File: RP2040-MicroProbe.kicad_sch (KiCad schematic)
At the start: 66 parts, among them J1 CONN_MCU_JTAG, J10 CONN_USB, J2 CONN_MCU_UART, J3 CONN_DBG_COMB, J4 CONN_3V3_JUMPER, J7 CONN_DBG_JTAG, SW1 BOOTSEL, U1 W25Q128JVS, U2 RP2040, U3 74AUP1T17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

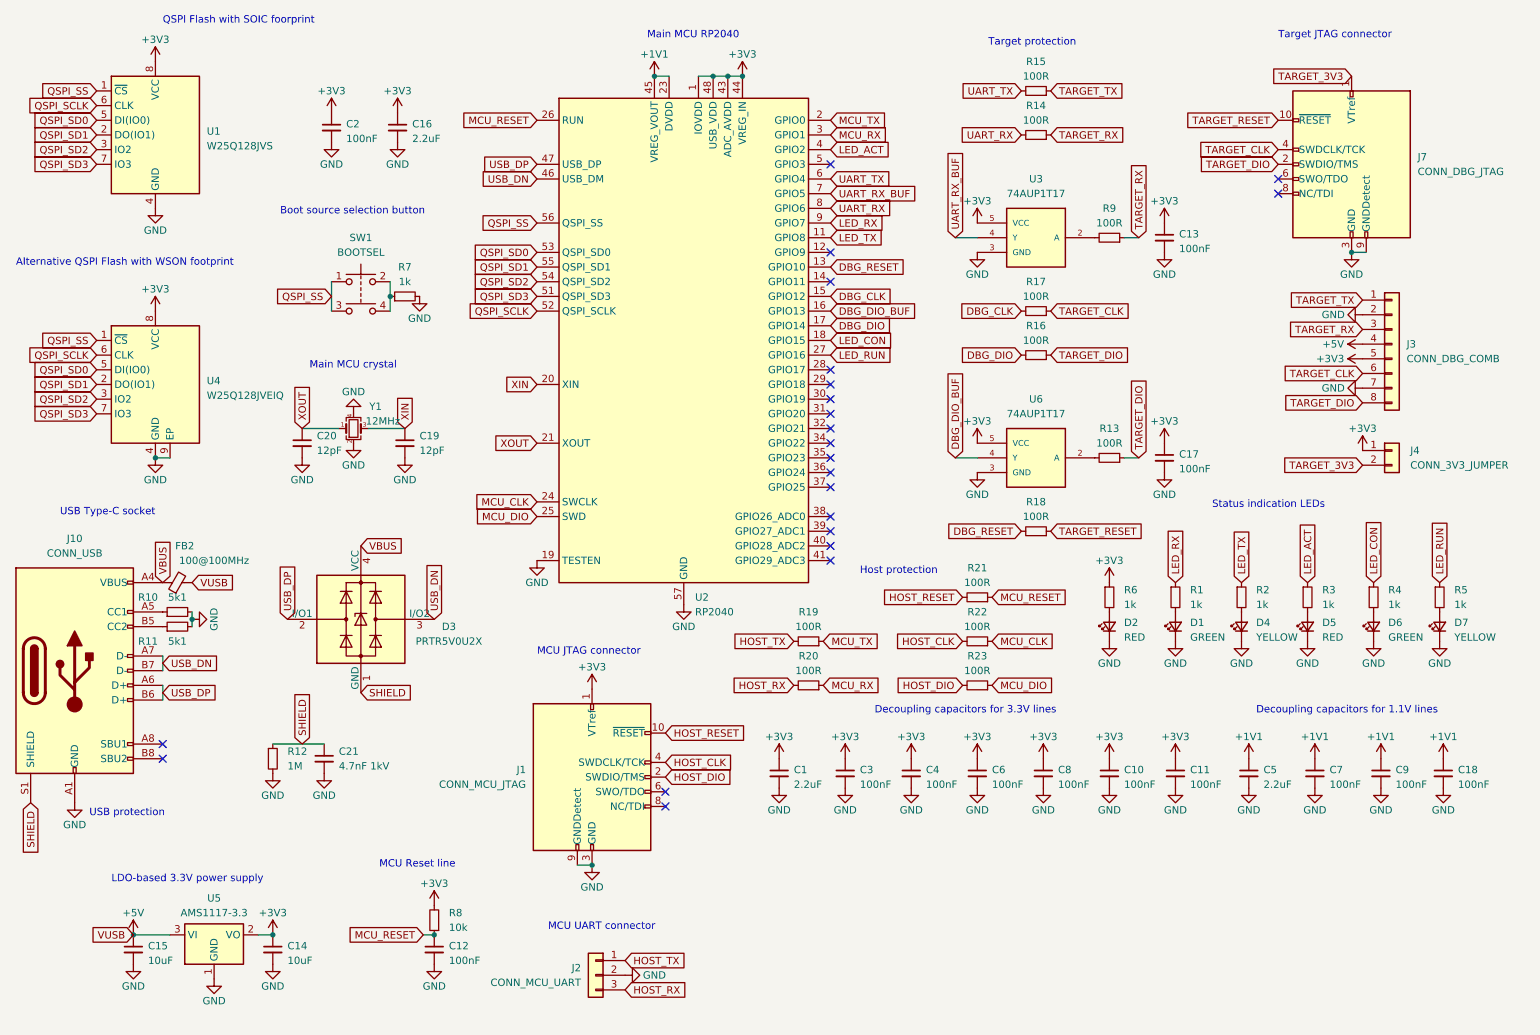
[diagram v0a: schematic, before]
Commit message: Cleanup components a bit. Changed few components and footprints.
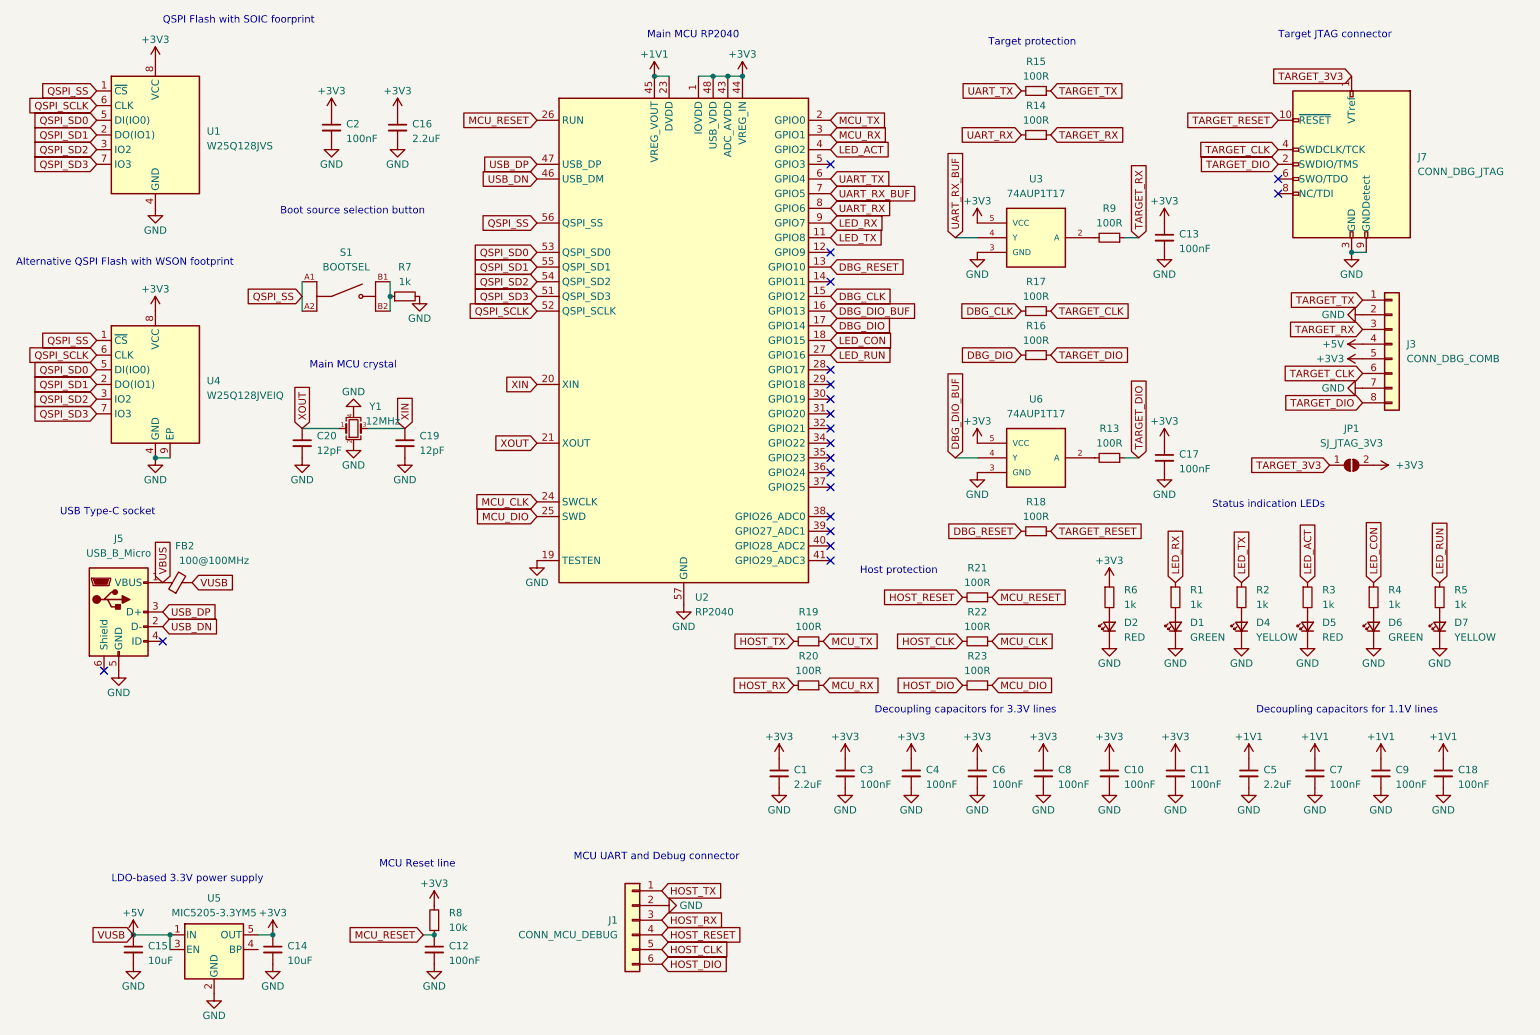
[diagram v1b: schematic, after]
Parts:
- removed C21: 4.7nF 1kV, Capacitor_SMD:C_1206_3216Metric, symbol Device:C_Small
- removed D3: PRTR5V0U2X, Package_TO_SOT_SMD:SOT-143, symbol Power_Protection:PRTR5V0U2X
- removed J1: CONN_MCU_JTAG, Connector_PinHeader_1.27mm:PinHeader_2x05_P1.27mm_Vertical, symbol Connector:Conn_ARM_JTAG_SWD_10
- removed J10: CONN_USB, Connector_USB:USB_C_Receptacle_HRO_TYPE-C-31-M-12, symbol Connector:USB_C_Receptacle_USB2.0
- removed J2: CONN_MCU_UART, Connector_PinHeader_2.54mm:PinHeader_1x03_P2.54mm_Vertical, symbol Connector_Generic:Conn_01x03
- removed J4: CONN_3V3_JUMPER, Connector_PinHeader_2.54mm:PinHeader_1x02_P2.54mm_Vertical, symbol Connector_Generic:Conn_01x02
- removed R10, R11: 5k1, Resistor_SMD:R_0402_1005Metric, symbol Device:R_Small
- removed R12: 1M, Resistor_SMD:R_0603_1608Metric, symbol Device:R_Small
- removed SW1: BOOTSEL, PCM_4ms_Switch:Button_Tact_Sqkg, symbol Switch:SW_Push_Dual
- removed U5: AMS1117-3.3, Package_TO_SOT_SMD:SOT-223-3_TabPin2, symbol Regulator_Linear:AMS1117-3.3
- added J1: CONN_MCU_DEBUG, Connector_PinHeader_2.54mm:PinHeader_1x06_P2.54mm_Vertical, symbol Connector_Generic:Conn_01x06
- added J5: USB_B_Micro, Connector_USB:USB_Micro-B_Molex_47346-0001, symbol Connector:USB_B_Micro
- added JP1: SJ_JTAG_3V3, Jumper:SolderJumper-2_P1.3mm_Open_TrianglePad1.0x1.5mm, symbol Jumper:SolderJumper_2_Open
- added S1: BOOTSEL, lib:SW_EVPBB0AAB000, symbol EVPBB0AAB000:EVPBB0AAB000
- added U5: MIC5205-3.3YM5, Package_TO_SOT_SMD:SOT-23-5, symbol Regulator_Linear:MIC5205-3.3YM5
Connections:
- net +3V3: now also JP1.2 (B), U5.5 (OUT)
- net +5V: now also U5.1 (IN), U5.3 (EN)
- net GND: now also J1.2 (Pin_2), J5.5 (GND), U5.2 (GND)
- net HOST_CLK: now also J1.5 (Pin_5)
- net HOST_DIO: now also J1.6 (Pin_6)
- net HOST_RESET: now also J1.4 (Pin_4)
- net HOST_RX: now also J1.3 (Pin_3)
- net HOST_TX: now also J1.1 (Pin_1)
- net QSPI_SS: now also S1.A1, S1.A2
- net TARGET_3V3: now also JP1.1 (A)
- net USB_DN: now also J5.2 (D-)
- net USB_DP: now also J5.3 (D+)
- net VBUS: now also J5.1 (VBUS)
- net at R7.1: now also S1.B1, S1.B2
- no-connect marks 22 -> 20
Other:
- note added: "MCU UART and Debug connector"
- note removed: "MCU JTAG connector"
- note removed: "MCU UART connector"
- note removed: "USB protection"
- title: RP2040-DebugProbe-0010 -> RP2040-MicroProbe-0010

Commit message: Moved stuff around
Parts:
- removed R19, R20, R21, R22, R23: 100R, Resistor_SMD:R_0402_1005Metric, symbol Device:R_Small
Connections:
- net MCU_CLK is gone; now on net HOST_CLK: U2.24 (SWCLK)
- net MCU_DIO is gone; now on net HOST_DIO: U2.25 (SWD)
- net MCU_RESET is gone; now on net HOST_RESET: C12.1, R8.1, U2.26 (RUN)
- net MCU_RX is gone; now on net HOST_RX: U2.3 (GPIO1)
- net MCU_TX is gone; now on net HOST_TX: U2.2 (GPIO0)
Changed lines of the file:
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@@
   (no_connect (at 166.37 101.6))
   (no_connect (at 166.37 45.72))
+  (wire (pts (xy 160.02 128.27) (xy 165.1 128.27))
+    (stroke (width 0) (type default))
+  )
   (wire (pts (xy 86.36 91.44) (xy 92.71 91.44))
     (stroke (width 0) (type default))
   )
+  (wire (pts (xy 160.02 135.89) (xy 165.1 135.89))
+    (stroke (width 0) (type default))
+  )
   (wire (pts (xy 219.71 96.52) (xy 217.17 96.52))
     (stroke (width 0) (type default))
   )
+  (wire (pts (xy 189.23 120.65) (xy 194.31 120.65))
+    (stroke (width 0) (type default))
+  )
   (wire (pts (xy 74.93 66.04) (xy 74.93 71.12))
     (stroke (width 0) (type default))
@@
     (stroke (width 0) (type default))
   )
+  (wire (pts (xy 189.23 135.89) (xy 194.31 135.89))
+    (stroke (width 0) (type default))
+  )
   (wire (pts (xy 95.885 179.07) (xy 97.79 179.07))
     (stroke (width 0) (type default))
@@
   )
   (wire (pts (xy 187.96 58.42) (xy 191.77 58.42))
+    (stroke (width 0) (type default))
+  )
+  (wire (pts (xy 189.23 128.27) (xy 194.31 128.27))
     (stroke (width 0) (type default))
   )
@@
         (path "/9a38a81c-7302-494f-9784-2ab4342a0a1d"
           (reference "#PWR031") (unit 1)
-        )
-      )
-    )
-  )
-  (symbol (lib_id "Device:R_Small") (at 162.56 135.89 270) (mirror x) (unit 1)
-    (in_bom yes) (on_board yes) (dnp no) (fields_autoplaced)
-    (property "Reference" "R20" (at 162.56 130.81 90)
-      (effects (font (size 1.27 1.27)))
-    )
-    (property "Value" "100R" (at 162.56 133.35 90)
-      (effects (font (size 1.27 1.27)))
-    )
-    (property "Footprint" "Resistor_SMD:R_0402_1005Metric" (at 162.56 135.89 0)
-      (effects (font (size 1.27 1.27)) hide)
-    )
-    (property "Datasheet" "~" (at 162.56 135.89 0)
-      (effects (font (size 1.27 1.27)) hide)
-    )
-    (pin "1")
-    (pin "2")
-    (instances
-      (project "RP2040-MicroProbe"
-        (path "/9a38a81c-7302-494f-9784-2ab4342a0a1d"
-          (reference "R20") (unit 1)
         )
       )
@@
     )
   )
-  (symbol (lib_id "Device:R_Small") (at 191.77 120.65 270) (mirror x) (unit 1)
-    (in_bom yes) (on_board yes) (dnp no) (fields_autoplaced)
-    (property "Reference" "R21" (at 191.77 115.57 90)
-      (effects (font (size 1.27 1.27)))
-    )
-    (property "Value" "100R" (at 191.77 118.11 90)
-      (effects (font (size 1.27 1.27)))
-    )
-    (property "Footprint" "Resistor_SMD:R_0402_1005Metric" (at 191.77 120.65 0)
-      (effects (font (size 1.27 1.27)) hide)
-    )
-    (property "Datasheet" "~" (at 191.77 120.65 0)
-      (effects (font (size 1.27 1.27)) hide)
-    )
-    (pin "1")
-    (pin "2")
-    (instances
-      (project "RP2040-MicroProbe"
-        (path "/9a38a81c-7302-494f-9784-2ab4342a0a1d"
-          (reference "R21") (unit 1)
-        )
-      )
-    )
-  )
   (symbol (lib_id "power:GND") (at 157.48 153.67 0) (unit 1)
     (in_bom yes) (on_board yes) (dnp no)
@@
     )
   )
-  (symbol (lib_id "Device:R_Small") (at 162.56 128.27 270) (mirror x) (unit 1)
-    (in_bom yes) (on_board yes) (dnp no) (fields_autoplaced)
-    (property "Reference" "R19" (at 162.56 123.19 90)
-      (effects (font (size 1.27 1.27)))
-    )
-    (property "Value" "100R" (at 162.56 125.73 90)
-      (effects (font (size 1.27 1.27)))
-    )
-    (property "Footprint" "Resistor_SMD:R_0402_1005Metric" (at 162.56 128.27 0)
-      (effects (font (size 1.27 1.27)) hide)
-    )
-    (property "Datasheet" "~" (at 162.56 128.27 0)
-      (effects (font (size 1.27 1.27)) hide)
-    )
-    (pin "1")
-    (pin "2")
-    (instances
-      (project "RP2040-MicroProbe"
-        (path "/9a38a81c-7302-494f-9784-2ab4342a0a1d"
-          (reference "R19") (unit 1)
-        )
-      )
-    )
-  )
   (symbol (lib_id "power:GND") (at 43.18 133.35 0) (unit 1)
     (in_bom yes) (on_board yes) (dnp no)
@@
         (path "/9a38a81c-7302-494f-9784-2ab4342a0a1d"
           (reference "R2") (unit 1)
-        )
-      )
-    )
-  )
-  (symbol (lib_id "Device:R_Small") (at 191.77 128.27 270) (mirror x) (unit 1)
-    (in_bom yes) (on_board yes) (dnp no) (fields_autoplaced)
-    (property "Reference" "R22" (at 191.77 123.19 90)
-      (effects (font (size 1.27 1.27)))
-    )
-    (property "Value" "100R" (at 191.77 125.73 90)
-      (effects (font (size 1.27 1.27)))
-    )
-    (property "Footprint" "Resistor_SMD:R_0402_1005Metric" (at 191.77 128.27 0)
-      (effects (font (size 1.27 1.27)) hide)
-    )
-    (property "Datasheet" "~" (at 191.77 128.27 0)
-      (effects (font (size 1.27 1.27)) hide)
-    )
-    (pin "1")
-    (pin "2")
-    (instances
-      (project "RP2040-MicroProbe"
-        (path "/9a38a81c-7302-494f-9784-2ab4342a0a1d"
-          (reference "R22") (unit 1)
         )
       )
@@
         )
       )
-    )
-  )
-  (symbol (lib_id "Device:R_Small") (at 191.77 135.89 270) (mirror x) (unit 1)
-    (in_bom yes) (on_board yes) (dnp no) (fields_autoplaced)
-    (property "Reference" "R23" (at 191.77 130.81 90)
-      (effects (font (size 1.27 1.27)))
-    )
-    (property "Value" "100R" (at 191.77 133.35 90)
-      (effects (font (size 1.27 1.27)))
-    )
-    (property "Footprint" "Resistor_SMD:R_0402_1005Metric" (at 191.77 135.89 0)
-      (effects (font (size 1.27 1.27)) hide)
-    )
-    (property "Datasheet" "~" (at 191.77 135.89 0)
-      (effects (font (size 1.27 1.27)) hide)
-    )
-    (pin "1")
-    (pin "2")
-    (instances
-      (project "RP2040-MicroProbe"
-        (path "/9a38a81c-7302-494f-9784-2ab4342a0a1d"
-          (reference "R23") (unit 1)
-        )
-      )

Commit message: Moved stuff around
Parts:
- removed C3, C7: 100nF, Capacitor_SMD:C_0402_1005Metric, symbol Device:C_Small
- removed J3: CONN_DBG_COMB, Connector_PinHeader_2.54mm:PinHeader_1x08_P2.54mm_Vertical, symbol Connector_Generic:Conn_01x08
- removed R13, R14, R15, R16, R17, R18, R9: 100R, Resistor_SMD:R_0402_1005Metric, symbol Device:R_Small
- added J2: CONN_DBG_COMB, Connector_PinSocket_2.54mm:PinSocket_1x07_P2.54mm_Vertical, symbol Connector_Generic:Conn_01x07
- added JP2: SJ_RESET, Jumper:SolderJumper-2_P1.3mm_Open_TrianglePad1.0x1.5mm, symbol Jumper:SolderJumper_2_Open
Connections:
- net TARGET_CLK is gone; now on net DBG_CLK: J7.4 (SWDCLK/TCK)
- net TARGET_DIO is gone; now on net DBG_DIO: J7.2 (SWDIO/TMS)
- net UART_RX is gone; now on net TARGET_RX: U2.8 (GPIO6)
- net UART_TX is gone; now on net TARGET_TX: U2.6 (GPIO4)
- net +3V3: now also J2.4 (Pin_4)
- net DBG_CLK: now also J2.5 (Pin_5)
- net DBG_DIO: now also U6.2 (A), J2.7 (Pin_7)
- net DBG_RESET: now also JP2.1 (A)
- net GND: now also J2.2 (Pin_2), J2.6 (Pin_6)
- net TARGET_RESET: now also JP2.2 (B)
- net TARGET_RX: now also U3.2 (A), J2.3 (Pin_3)
- net TARGET_TX: now also J2.1 (Pin_1)
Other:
- note added: "Host connections"
- note added: "Target connections"
- note removed: "Host protection"
- note removed: "Target protection"
- moved on the sheet: C1, C13, C17, C18, C9

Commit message: Moved stuff around
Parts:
- J7: footprint Connector_PinHeader_1.27mm:PinHeader_2x05_P1.27mm_Vertical -> Connector_PinHeader_1.27mm:PinHeader_2x05_P1.27mm_Vertical_SMD
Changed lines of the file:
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@@
       (effects (font (size 1.27 1.27)) (justify right))
     )
-    (property "Footprint" "Connector_PinHeader_1.27mm:PinHeader_2x05_P1.27mm_Vertical" (at 256.54 45.72 0)
+    (property "Footprint" "Connector_PinHeader_1.27mm:PinHeader_2x05_P1.27mm_Vertical_SMD" (at 256.54 45.72 0)
       (effects (font (size 1.27 1.27)) hide)
     )

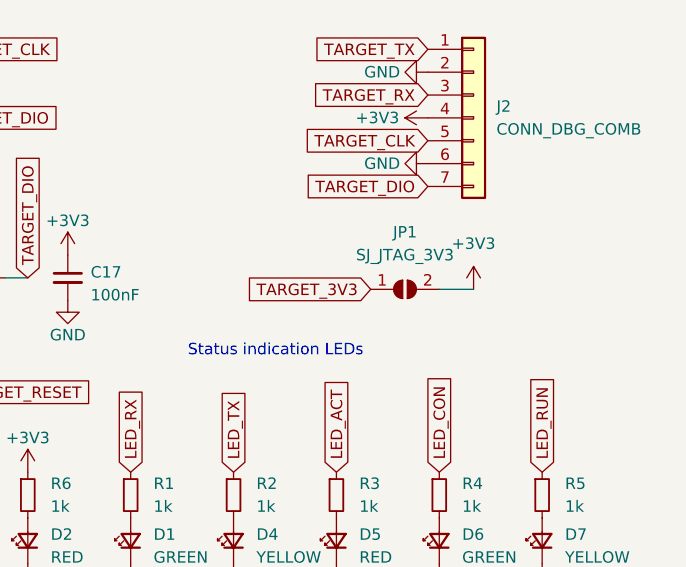
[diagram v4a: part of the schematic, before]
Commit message: Added traces and vias
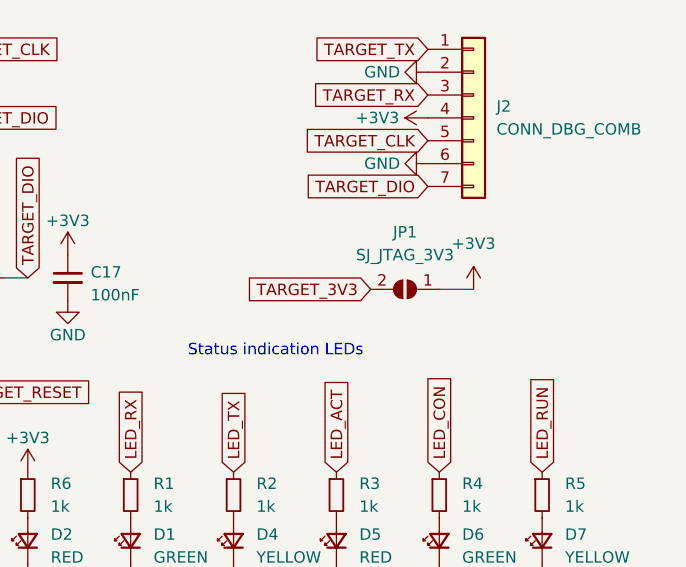
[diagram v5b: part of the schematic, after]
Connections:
- net +3V3: now also JP1.1 (A); no longer JP1.2 (B)
- net TARGET_3V3: now also JP1.2 (B); no longer JP1.1 (A)
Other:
- moved on the sheet: JP1
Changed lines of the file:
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@@
   (title_block
     (title "RP2040-MicroProbe-0010")
-    (date "2023-12-18")
+    (date "2023-12-19")
     (rev "1.0")
     (company "(c) 2023 Andriy Golovnya")
@@
     )
   )
-  (symbol (lib_id "Jumper:SolderJumper_2_Open") (at 256.54 97.79 0) (unit 1)
+  (symbol (lib_id "Jumper:SolderJumper_2_Open") (at 256.54 97.79 180) (unit 1)
     (in_bom yes) (on_board yes) (dnp no) (fields_autoplaced)
     (property "Reference" "JP1" (at 256.54 91.44 0)

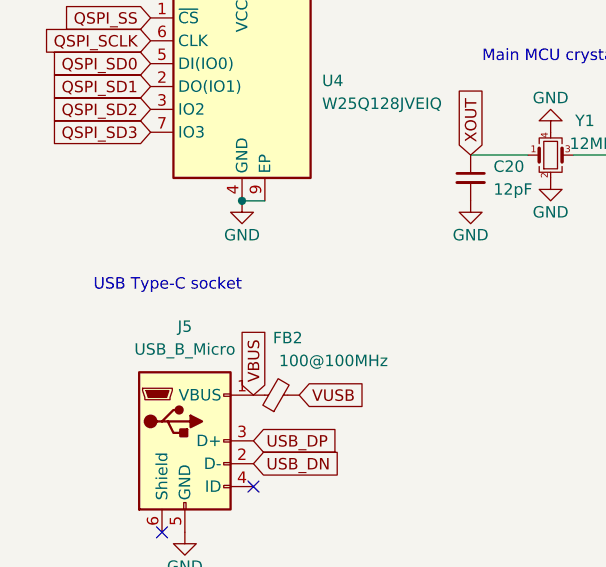
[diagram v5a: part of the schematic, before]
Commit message: Fixes a typo in schematics
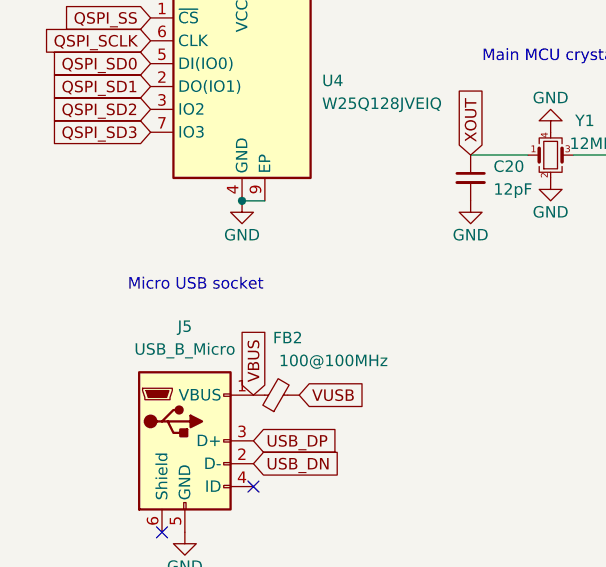
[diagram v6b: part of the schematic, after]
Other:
- note added: "Micro USB socket"
- note removed: "USB Type-C socket"
- company: (c) 2023 Andriy Golovnya -> (c) 2023-2024 Andriy Golovnya
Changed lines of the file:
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@@
   (title_block
     (title "RP2040-MicroProbe-0010")
-    (date "2023-12-19")
+    (date "2024-01-08")
     (rev "1.0")
-    (company "(c) 2023 Andriy Golovnya")
+    (company "(c) 2023-2024 Andriy Golovnya")
     (comment 1 "RP2040 based Micro Debug Probe")
     (comment 2 "Designed in Germany")
@@
     (effects (font (size 1.27 1.27)) (justify left bottom))
   )
-  (text "USB Type-C socket" (at 33.02 106.68 0)
+  (text "Micro USB socket" (at 36.83 106.68 0)
     (effects (font (size 1.27 1.27)) (justify left bottom))
   )
